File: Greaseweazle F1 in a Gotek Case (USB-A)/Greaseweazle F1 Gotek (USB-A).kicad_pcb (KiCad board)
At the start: 2 copper layers, 111.6 x 68.1 mm, 45 parts, among them CN1 FLOPPY, J1 USB A, J2 Floppy Power, J3 Programming Port, U1 Blue Pill

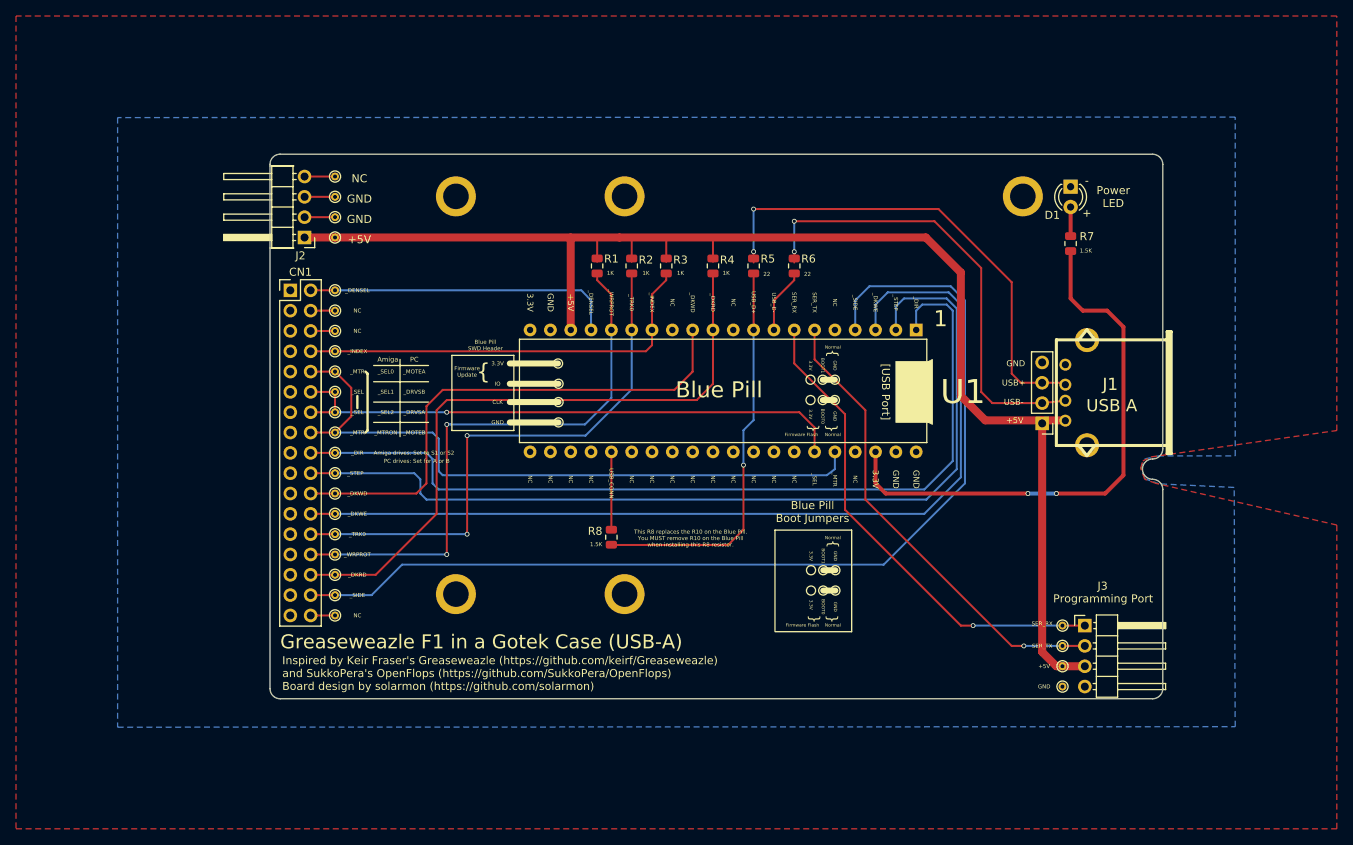
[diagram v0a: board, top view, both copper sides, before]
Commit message: Added through hole resistor footprints
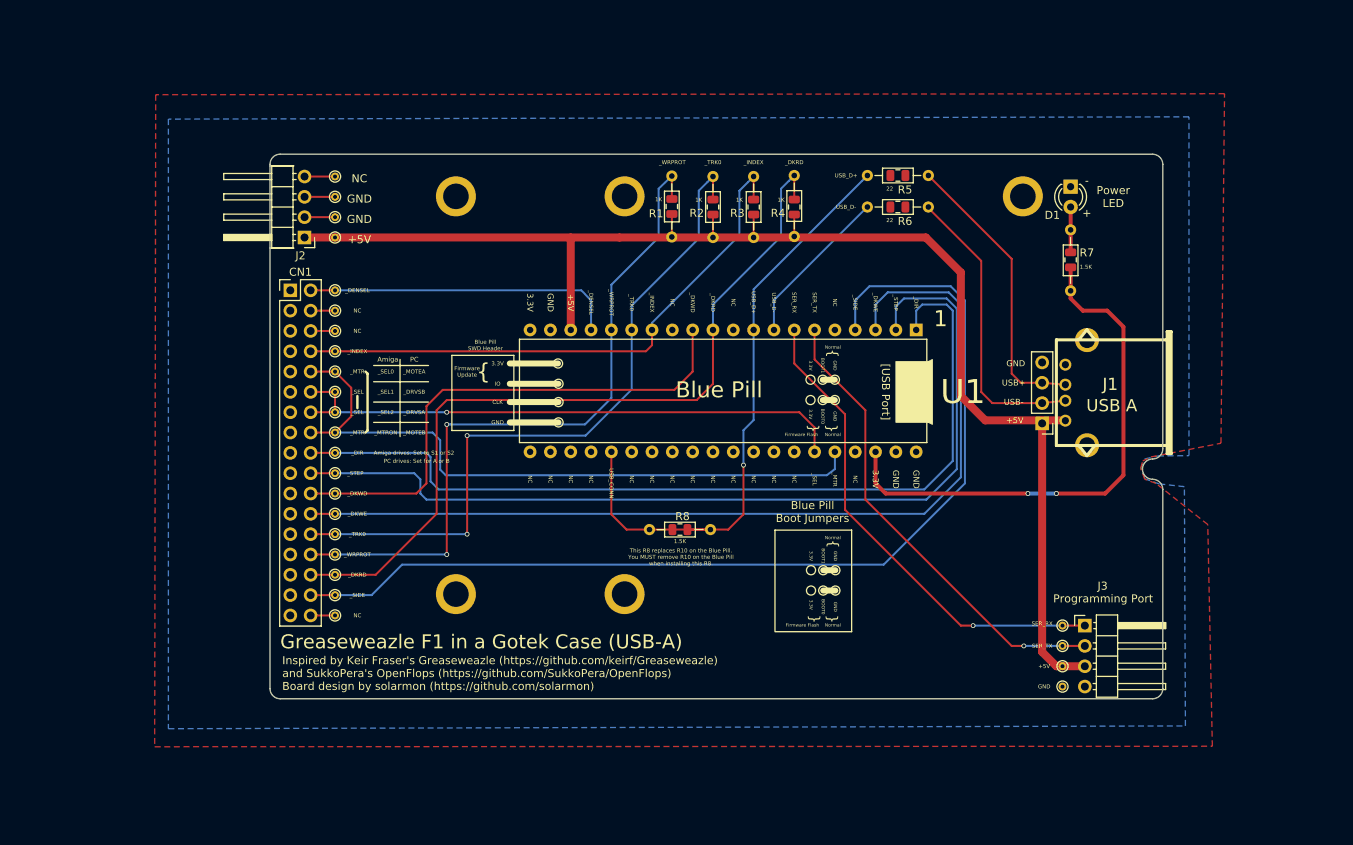
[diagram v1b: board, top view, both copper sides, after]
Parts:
- added ?: R_Axial_DIN0204_L3.6mm_D1.6mm_P7.62mm_Horizontal, Resistor_THT:R_Axial_DIN0204_L3.6mm_D1.6mm_P7.62mm_Horizontal, F.Cu at (177.5, 62.0)
- added ?: R_Axial_DIN0204_L3.6mm_D1.6mm_P7.62mm_Horizontal, Resistor_THT:R_Axial_DIN0204_L3.6mm_D1.6mm_P7.62mm_Horizontal, F.Cu at (177.5, 58.0)
- added ?: R_Axial_DIN0204_L3.6mm_D1.6mm_P7.62mm_Horizontal, Resistor_THT:R_Axial_DIN0204_L3.6mm_D1.6mm_P7.62mm_Horizontal, F.Cu at (160.8, 65.7)
- added ?: R_Axial_DIN0204_L3.6mm_D1.6mm_P7.62mm_Horizontal, Resistor_THT:R_Axial_DIN0204_L3.6mm_D1.6mm_P7.62mm_Horizontal, F.Cu at (155.7, 65.8)
- added ?: R_Axial_DIN0204_L3.6mm_D1.6mm_P7.62mm_Horizontal, Resistor_THT:R_Axial_DIN0204_L3.6mm_D1.6mm_P7.62mm_Horizontal, F.Cu at (150.6, 65.8)
- added ?: R_Axial_DIN0204_L3.6mm_D1.6mm_P7.62mm_Horizontal, Resistor_THT:R_Axial_DIN0204_L3.6mm_D1.6mm_P7.62mm_Horizontal, F.Cu at (145.5, 65.7)
- added ?: R_Axial_DIN0204_L3.6mm_D1.6mm_P7.62mm_Horizontal, Resistor_THT:R_Axial_DIN0204_L3.6mm_D1.6mm_P7.62mm_Horizontal, F.Cu at (150.3, 102.3)
- added ?: R_Axial_DIN0204_L3.6mm_D1.6mm_P7.62mm_Horizontal, Resistor_THT:R_Axial_DIN0204_L3.6mm_D1.6mm_P7.62mm_Horizontal, F.Cu at (195.3, 64.8)
- moved R5 21.3 mm to (173.7, 58.0), turned to 180 degrees
- moved R6 14.9 mm to (173.7, 62.0), turned to 180 degrees
- moved R3 13.2 mm to (155.7, 62.0), turned to 90 degrees
- moved R2 12.5 mm to (150.6, 62.0), turned to 90 degrees
- moved R4 12.5 mm to (160.8, 62.0), turned to 90 degrees
- moved R1 11.9 mm to (145.5, 61.9), turned to 90 degrees
- moved R8 8.63 mm to (146.5, 102.3), turned to 180 degrees
- moved R7 2.03 mm to (195.3, 68.6)
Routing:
- net Net-(J1-Pad3): track 61.4 -> 36.3 mm, vias 2 -> 0
- net Net-(J1-Pad2): track 57.6 -> 37.0 mm, vias 2 -> 0
- net /_TRK0: track 68.8 -> 88.5 mm
- net /_INDEX: track 52.7 -> 72.2 mm
- net /_DKRD: track 82.8 -> 101.0 mm
- net /_WRPROT: track 71.5 -> 89.0 mm
- net /USB_D-: track 8.12 -> 20.2 mm
- net /USB_D+: track 49.9 -> 61.5 mm
- net /USB_CONN: track 9.78 -> 16.0 mm
- net +3V3: track 68.9 -> 66.9 mm
- net Net-(D1-Pad2): track 3.63 -> 5.67 mm
- net +5V: track 173.0 -> 171.6 mm
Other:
- board text added: "This R8 replaces R10 on the Blue Pill. You MUST remove R10 on the Blue Pill when installing this R8."
- board text removed: "This R8 replaces the R10 on the Blue Pill. You MUST remove R10 on the Blue Pill when installing this R8 resistor."

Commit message: Added features
* Added Activity LED
* Added resistor pack
* Added Blue Pill footprint
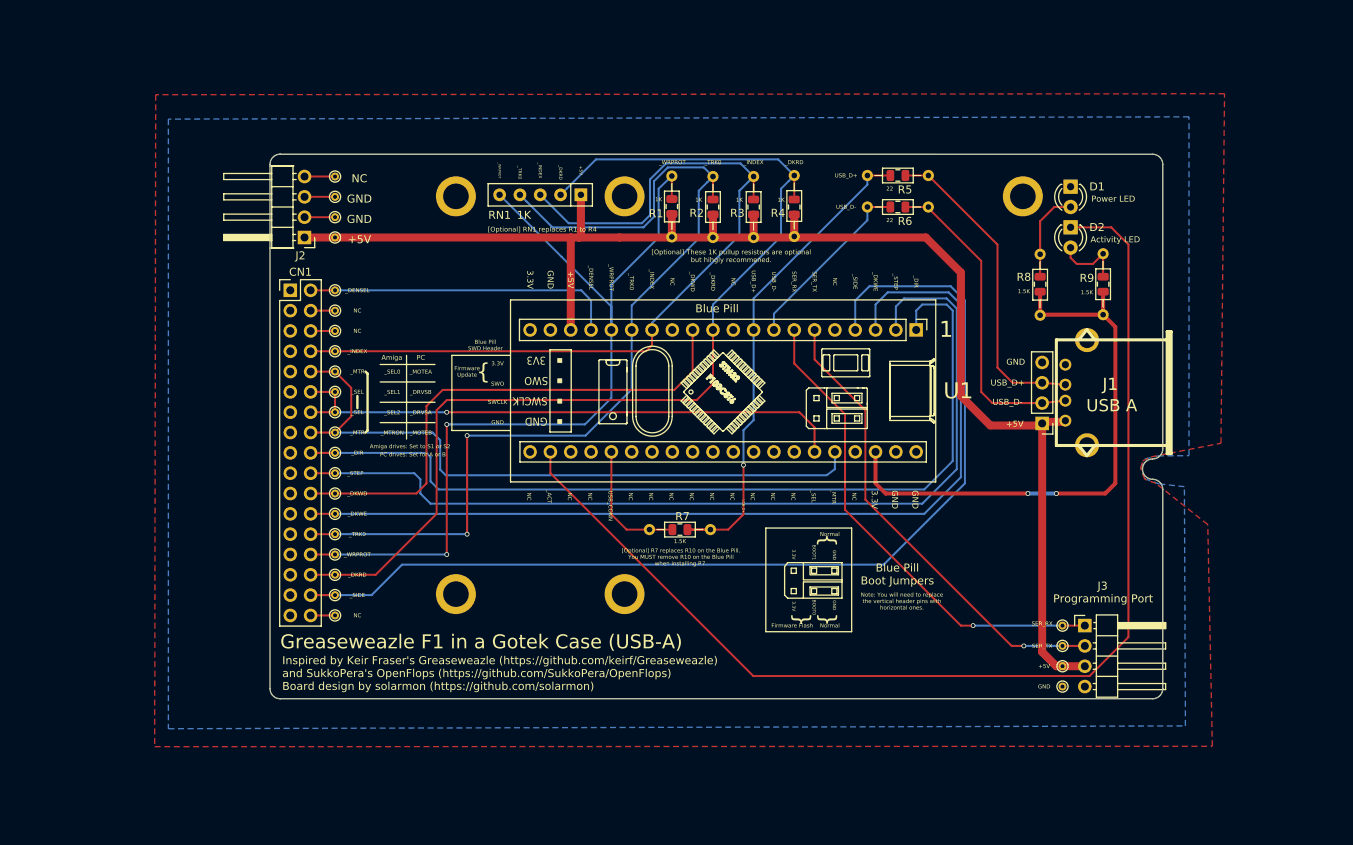
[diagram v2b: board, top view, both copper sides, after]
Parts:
- added ?: R_Axial_DIN0204_L3.6mm_D1.6mm_P7.62mm_Horizontal, Resistor_THT:R_Axial_DIN0204_L3.6mm_D1.6mm_P7.62mm_Horizontal, F.Cu at (199.4, 67.8)
- added D2: LED, LED_THT:LED_D3.0mm, F.Cu at (195.3, 64.5)
- added R9: 1.5K, Resistor_SMD:R_0805_2012Metric, F.Cu at (199.4, 71.6)
- added RN1: 1K, Resistor_THT:R_Array_SIP5, F.Cu at (134.1, 60.5)
- U1: footprint Package_DIP:DIP-40_W15.24mm -> Kicad-STM32-master:YAAJ_BluePill_1
- moved ? 4.88 mm to (191.5, 67.9)
- moved R8 4.88 mm to (191.5, 71.6)
- renumbered R8 to R7, R7 to R8
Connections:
- R3 pad 1: +5V -> Net-(R3-Pad1)
- U1 pad 22: Net-(U1-Pad22) -> /_ACT
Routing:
- net /_ACT: track 0.00 -> 144.6 mm
- net /_INDEX: track 72.2 -> 106.7 mm
- net /_TRK0: track 88.5 -> 120.5 mm
- net /_DKRD: track 101.0 -> 132.9 mm
- net /_WRPROT: track 89.0 -> 111.7 mm
- net Net-(D2-Pad2): track 0.00 -> 9.05 mm
- net Net-(D1-Pad2): track 5.67 -> 11.5 mm
- net +5V: track 171.6 -> 177.2 mm
- net +3V3: track 66.9 -> 70.4 mm
- net Net-(J1-Pad3): track 36.3 -> 39.7 mm
- net Net-(J1-Pad2): track 37.0 -> 39.9 mm
- net /USB_D-: track 20.2 -> 23.1 mm
- net /USB_D+: track 61.5 -> 62.5 mm
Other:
- board text added: "Activity LED"
- board text added: "Note: You will need to replace the vertical header pins with horizontal ones."
- board text added: "SWCLK"
- board text added: "SWO"
- board text added: "[Optional] R7 replaces R10 on the Blue Pill. You MUST remove R10 on the Blue Pill when installing R7."
- board text added: "[Optional] RN1 replaces R1 to R4"
- board text added: "[Optional] These 1K pullup resistors are optional but hihgly recommened."
- board text added: "_ACT"
- board text removed: "+"
- board text removed: "-"
- board text removed: "Blue Pill"
- board text removed: "CLK"
- board text removed: "IO"
- board text removed: "This R8 replaces R10 on the Blue Pill. You MUST remove R10 on the Blue Pill when installing this R8."
- board text removed: "USB+"
- board text removed: "USB-"
- board text removed: "[USB Port]"

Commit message: More improvements and corrections
* moved USB header
* Reset switch
* Corrected SWD labelling
* Added DPDT On-On-On toggle switch silk screen
* Cleaned up LED silk screen
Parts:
- added SW1: Reset, OpenFlops:PUSH_BUTTON_RIGHT_ANGLE, F.Cu at (203.2, 60.2)
- CN1: value FLOPPY -> Floppy Data
- D1, D2: footprint LED_THT:LED_D3.0mm -> Greaseweazle F1 in a Gotek Case (USB-A):LED_D3.0mm_Horizontal_O6.35mm_Z10.0mm_NoSilkS
- J1: renamed from ?; footprint Connector_PinHeader_2.54mm:PinHeader_1x04_P2.54mm_Vertical -> Connector_PinHeader_2.54mm:PinHeader_1x04_P2.54mm_Horizontal
- moved J1 12.3 mm to (204.0, 88.7)
- moved R9 7.89 mm to (191.5, 67.0)
- moved R9 7.89 mm to (191.5, 70.8)
- moved R8 4.22 mm to (187.4, 70.8)
- moved R8 4.22 mm to (187.4, 67.1)
- moved R1 2.67 mm to (148.1, 65.7)
- moved R1 2.67 mm to (148.1, 61.9)
- moved R3 2.67 mm to (158.4, 65.8)
- moved R3 2.67 mm to (158.4, 62.0)
- moved R4 2.67 mm to (163.4, 65.7)
- moved R4 2.67 mm to (163.4, 62.0)
- moved R2 2.67 mm to (153.3, 65.8)
- moved R2 2.67 mm to (153.3, 62.0)
- moved D1 2.59 mm to (195.3, 62.0), turned to 90 degrees
- moved D2 2.57 mm to (195.3, 67.1), turned to 90 degrees
- gave numbers to parts that had none: 9
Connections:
- R3 pad 1: Net-(R3-Pad1) -> +5V
- U1 pad 37: Net-(U1-Pad37) -> /_RST
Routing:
- net /_RST: track 0.00 -> 63.4 mm
- net +3V3: track 70.4 -> 48.8 mm
- net Net-(J1-Pad3): track 39.7 -> 50.4 mm
- net Net-(J1-Pad2): track 39.9 -> 49.3 mm
- net +5V: track 177.2 -> 186.5 mm
- net /_ACT: track 144.6 -> 138.2 mm
- net /_DKRD: track 132.9 -> 138.9 mm
- net /_INDEX: track 106.7 -> 112.1 mm
- net Net-(D1-Pad2): track 11.5 -> 16.4 mm
- net /_TRK0: track 120.5 -> 124.3 mm
- net /SER_RX: track 61.1 -> 62.9 mm
- net /_WRPROT: track 111.7 -> 112.8 mm
- net /_SIDE: track 129.3 -> 128.4 mm
- net Net-(D2-Pad2): track 9.05 -> 8.54 mm
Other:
- board text added: "(BOOT0) 3.3V"
- board text added: "(BOOT0) GND"
- board text added: "(SWD) GND"
- board text added: "(SWD) SWCLK"
- board text added: "Activity"
- board text added: "Firmware Program"
- board text added: "Power"
- board text added: "[Optional]"
- board text added: "[Optional] R1 to R4 1K pullup resistors are optional but highly recommened."
- board text added: "[Optional] RN1 replaces R1 to R4."
- board text added: "[Optional] SPDT On-On-On Toggle Switch"
- board text added: "[Optional] USB Header"
- board text added: "_RST"
- board text removed: "Activity LED"
- board text removed: "Firmware Flash"
- board text removed: "Power LED"
- board text removed: "[Optional] RN1 replaces R1 to R4"
- board text removed: "[Optional] These 1K pullup resistors are optional but hihgly recommened."

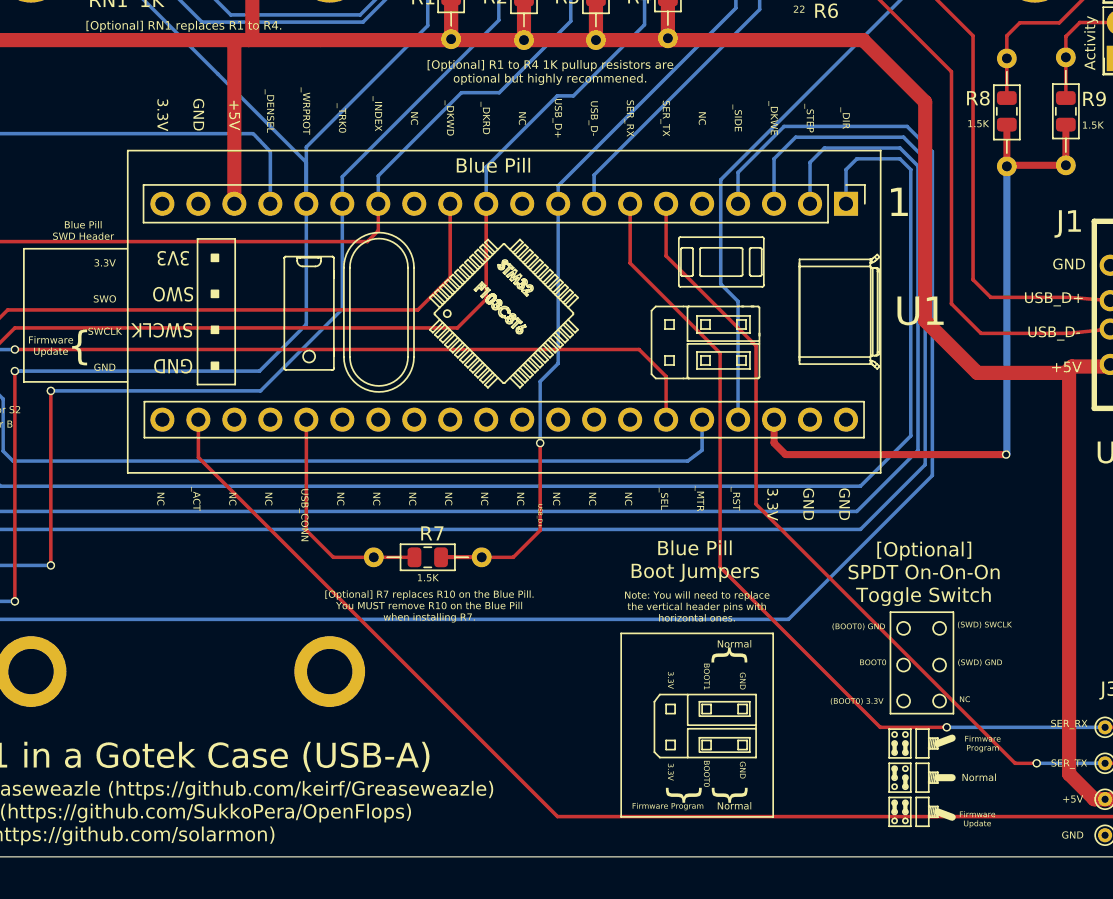
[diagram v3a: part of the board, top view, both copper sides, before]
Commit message: Added 3D models of Blue Pill and USB A and made some silk screen corrections
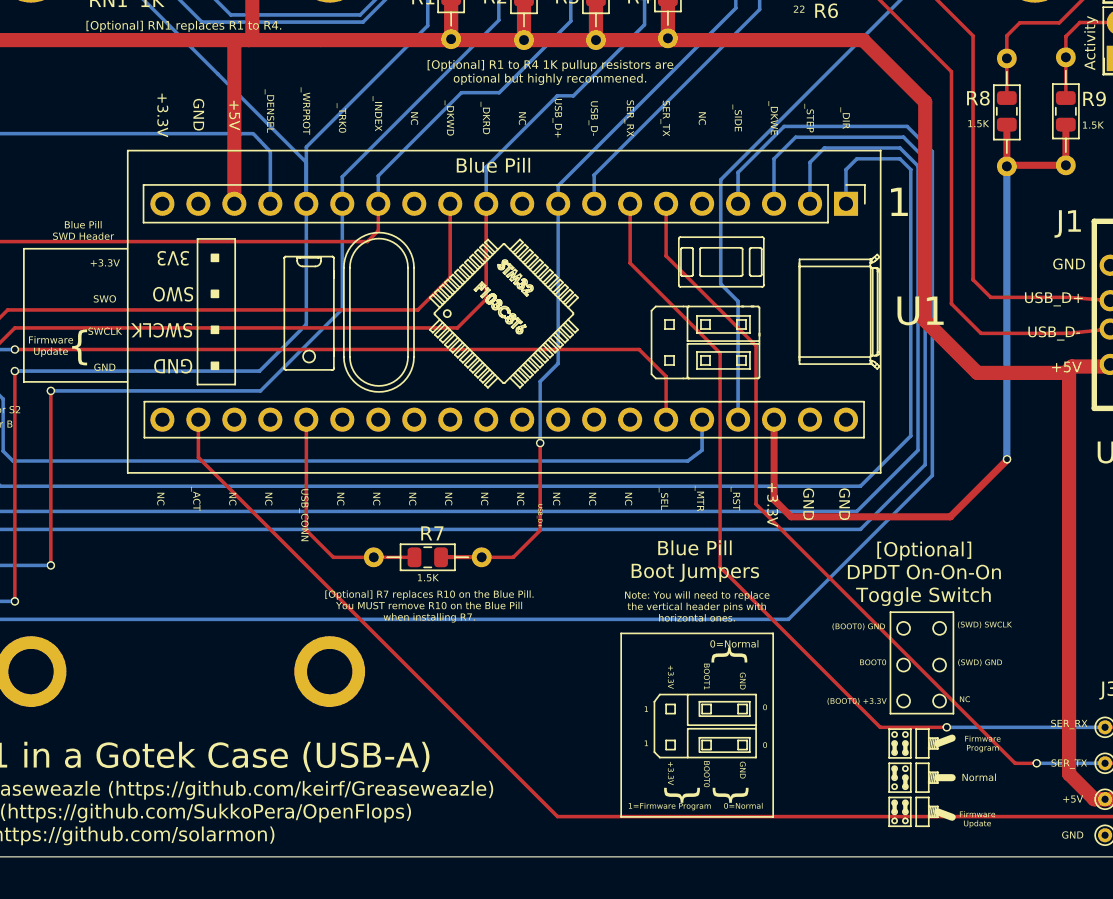
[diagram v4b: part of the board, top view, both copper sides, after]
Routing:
- net +3V3: track 48.8 -> 55.0 mm
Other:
- board text added: "(BOOT0) +3.3V"
- board text added: "+3.3V"
- board text added: "0"
- board text added: "0=Normal"
- board text added: "1=Firmware Program"
- board text added: "[Optional] DPDT On-On-On Toggle Switch"
- board text removed: "(BOOT0) 3.3V"
- board text removed: "3.3V"
- board text removed: "[Optional] SPDT On-On-On Toggle Switch"

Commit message: Tweaks and gerber files
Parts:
- D1, D2: footprint Greaseweazle F1 in a Gotek Case (USB-A):LED_D3.0mm_Horizontal_O6.35mm_Z10.0mm_NoSilkS -> LED_THT:LED_D3.0mm_Horizontal_O6.35mm_Z10.0mm
